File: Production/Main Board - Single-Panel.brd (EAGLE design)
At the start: 186.9 x 99.3 mm, 182 parts, among them J1 MICROMOD-2222-C, J10 MICRO-SD-PUSH-PUSH-EXT-PIN, J11 MICROMOD-2222-C, J12 CORTEX_JTAG_DEBUG_MINIMUM_PTH, J15 MICROMOD_CARRIER, J16 MICRO-SD-PUSH-PUSH-EXT-PIN, J2 Vertical Qwiic Connector, J4 QWIIC_RIGHT_ANGLE, J5 CORTEX_JTAG_DEBUG_MINIMUM_PTH, J6 MICROMOD_CARRIER, J7 Vertical Qwiic Connector, J9 QWIIC_RIGHT_ANGLE, Q1 3.1A/30V/105mΩ, Q2 3.1A/30V/105mΩ, U1 AP7361C-33, U2 MCP73831, U3 MCP73831, U5 AP7361C-33

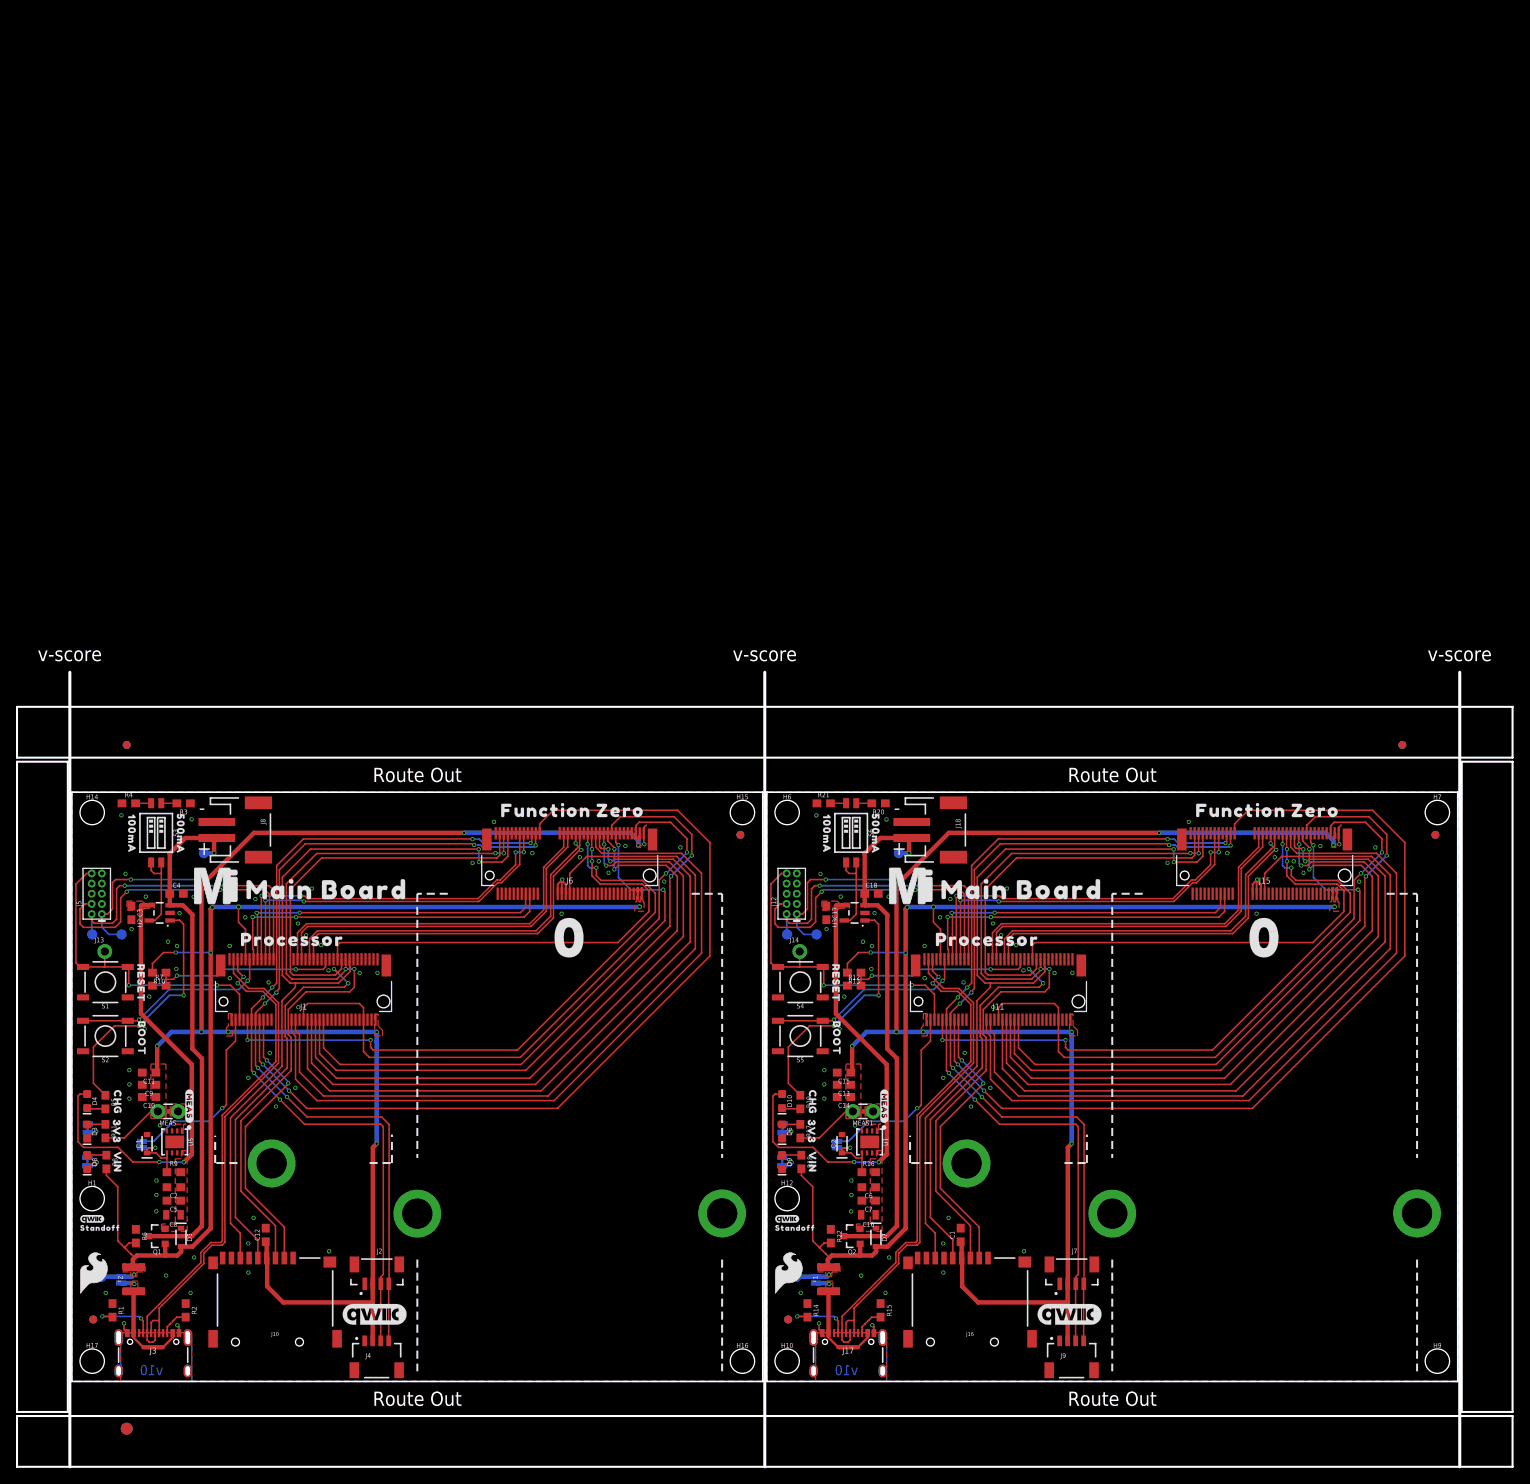
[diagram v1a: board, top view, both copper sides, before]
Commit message: Adds a larger manufacturing panel than the previous
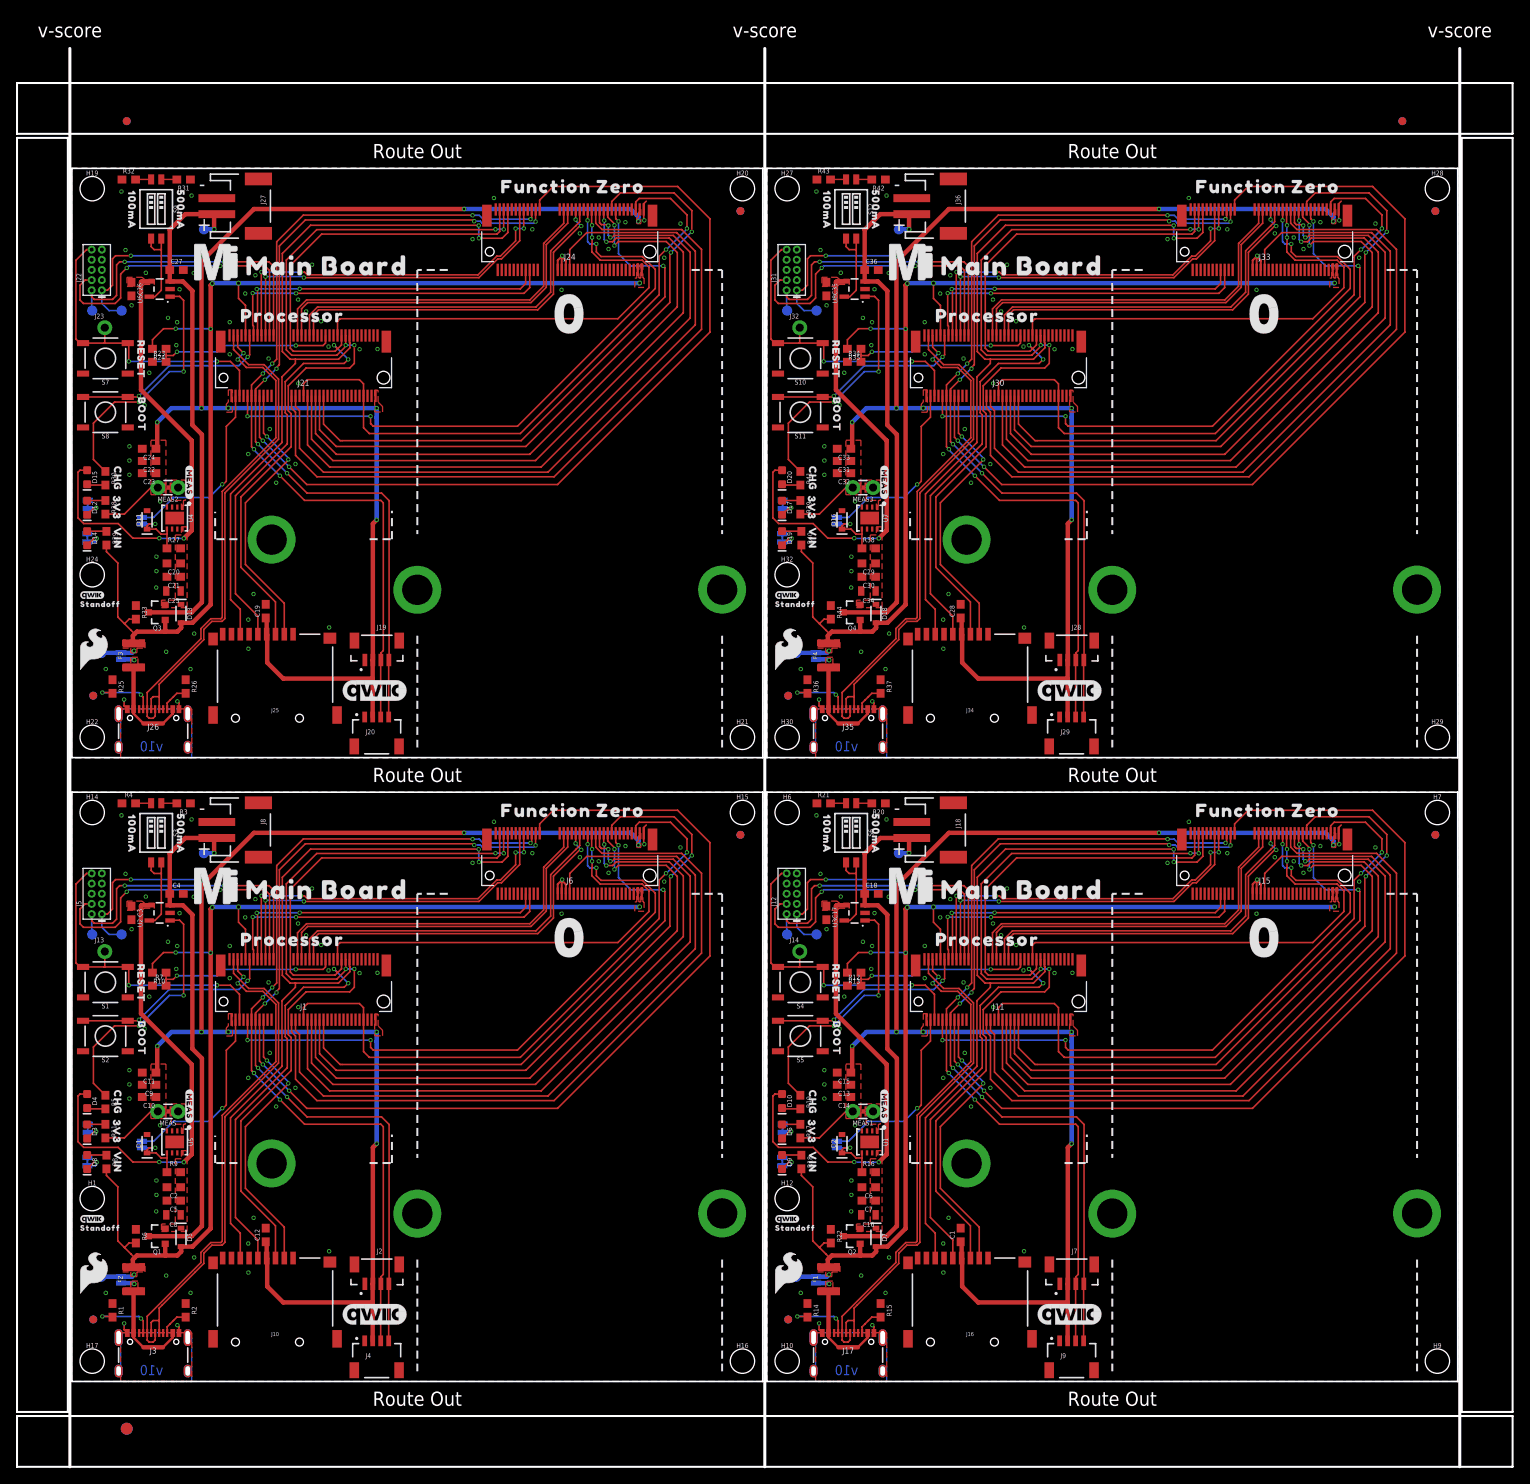
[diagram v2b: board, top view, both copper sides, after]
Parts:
- added 3V3_LED2, 3V3_LED3, 5V_LED2, 5V_LED3: (no value), SparkFun-Jumpers:SMT-JUMPER_2_NC_TRACE_SILK
- added BYP2, BYP3: JUMPER-SMT_2_NO_SILK, SparkFun-Jumpers:SMT-JUMPER_2_NO_SILK
- added C19, C21, C23, C28, C30, C32: 0.1uF, SparkFun-Capacitors:0603
- added C20, C24, C29, C33: 0.22uF, SparkFun-Capacitors:0603
- added C22, C31: 1.0uF, SparkFun-Capacitors:0603
- added C25, C34: 10uF, SparkFun-Capacitors:0805
- added C26, C27, C35, C36: 4.7uF, SparkFun-Capacitors:0603
- added D11, D16: 3.3V, SparkFun-DiscreteSemi:SOD-323
- added D12, D14, D17, D19: RED, SparkFun-LED:LED-0603
- added D13, D18: 3A/10V/280mV, SparkFun-DiscreteSemi:SOD-323
- added D15, D20: Yellow, SparkFun-LED:LED-0603
- added F3, F4: 6V/2A, SparkFun-Fuses:1210
- added FD10, FD11, FD12, FD13, FD14, FD15, FD16, FD9: FIDUCIAL1X2, SparkFun-Aesthetics:FIDUCIAL-1X2
- added H13, H18, H23, H25, H26, H31: STAND-OFF-REFLOW-M2.5_2.5MM_TALL, SparkFun-Hardware:STAND-OFF-REFLOW-M2.5
- added H19, H20, H21, H22, H24, H27, H28, H29, H30, H32: STAND-OFFTIGHT, SparkFun-Hardware:STAND-OFF-TIGHT
- added J19, J28: Vertical Qwiic Connector, SparkFun-Connectors:JST04_1MM_VERT
- added J20, J29: QWIIC_RIGHT_ANGLE, SparkFun-Connectors:JST04_1MM_RA
- added J21, J30: MICROMOD-2222-C, SparkFun-MicroMod:M.2-CONNECTOR-E
- added J22, J31: CORTEX_JTAG_DEBUG_MINIMUM_PTH, SparkFun-Connectors:2X5-PTH-1.27MM
- added J23, J32: (no value), SparkFun-Connectors:1X01_NO_SILK
- added J24, J33: MICROMOD_CARRIER, SparkFun-MicroMod-Function:M.2-CONNECTOR-E-FUNCTION-STANDARD
- added J25, J34: MICRO-SD-PUSH-PUSH-EXT-PIN, SparkFun-Connectors:MICROSD-EXTERNALPIN
- added J26, J35: (no value), SparkFun-Connectors:USB-C-16P-2LAYER-PADS
- added J27, J36: (no value), SparkFun-Connectors:JST-2-SMD
- added LOGO10, LOGO7: QWIIC_LOGO_8MM, SparkFun-Aesthetics:QWIIC_8MM
- added LOGO11, LOGO8: SFE_LOGO_NAME_FLAME.3_INCH, SparkFun-Aesthetics:SFE_LOGO_NAME_FLAME_.3
- added LOGO12, LOGO9: OSHW-LOGOL, SparkFun-Aesthetics:OSHW-LOGO-L
- added MEAS2, MEAS3: JUMPER-COMBO_2_NC_TRACE, SparkFun-Jumpers:COMBO-JUMPER_2_NC_TRACE
- added Q3, Q4: 3.1A/30V/105mΩ, SparkFun-DiscreteSemi:SOT23-3
- added R23, R32, R33, R34, R43, R44: 10k, SparkFun-Resistors:0603
- added R24, R35: 20k, SparkFun-Resistors:0603
- added R25, R26, R36, R37: 5.1k, SparkFun-Resistors:0603
- added R27, R38: 100k, SparkFun-Resistors:0603
- added R28, R30, R39, R41: 1k, SparkFun-Resistors:0603
- added R29, R40: 4.7k, SparkFun-Resistors:0603
- added R31, R42: 2.0k, SparkFun-Resistors:0603
- added S10, S7: Reset, SparkFun-Switches:TACTILE_SWITCH_SMD_5.2MM
- added S11, S8: BOOT, SparkFun-Switches:TACTILE_SWITCH_SMD_5.2MM
- added S12, S9: DIP-02-SMD-50MIL, SparkFun-Switches:DIPSWITCH-02-50MIL
- added TP10, TP11, TP12, TP13, TP14, TP15, TP16, TP9: TEST-POINT3X5, SparkFun-Connectors:PAD.03X.05
- added U$47, U$70: (no value), top:3V332530
- added U$48, U$71: (no value), top:VIN32529
- added U$49, U$72: (no value), top:CHG32528
- added U$50, U$73: (no value), top:FUNCTION_ZERO517
- added U$51, U$74: (no value), top:PROCESSOR522
- added U$52, U$75: (no value), top:#3V3_LED#17
- added U$53, U$76: (no value), top:#VIN_LED#16
- added U$54, U$77: (no value), top:#PTC#18
- added U$55, U$78: (no value), top:BOOT32541
- added U$56, U$79: (no value), top:RESET32540
- added U$57, U$80: (no value), top:#3V3_EN#18
- added U$58, U$81: (no value), SparkFun-MicroMod:MICROMOD_MI_LOGO_1
- added U$59, U$82: (no value), top:0525
- added U$60, U$83: (no value), top:MAIN523
- added U$61, U$84: (no value), top:BOARD524
- added U$62, U$85: (no value), top:100MA6
- added U$63, U$86: (no value), top:500MA101
- added U$64, U$87: (no value), top:MAIN_BOARD5523
- added U$65, U$88: (no value), SparkFun-MicroMod:MICROMOD_LOGO_1
- added U$66, U$89: (no value), SparkFun-Aesthetics:QWIIC_3MM
- added U$67, U$90: (no value), top:STANDOFF501
- added U$68, U$91: (no value), SparkFun-Aesthetics:SFE_LOGO_FLAME_.2
- added U$69, U$92: (no value), top:#MEAS#40313513
- added U4, U7: AP7361C-33, SparkFun-IC-Power:UDFN-8
- added U6, U8: MCP73831, SparkFun-IC-Power:SOT23-5
- added VE2, VE3: (no value), SparkFun-Jumpers:SMT-JUMPER_2_NO_SILK
- moved E$1 78.0 mm to (6.86, 157.5)
- moved E$2 78.0 mm to (6.86, 157.5)
- moved E$3 78.0 mm to (166.3, 157.5)
- moved E$4 78.0 mm to (166.3, 157.5)
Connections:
- new net !BOOT!2: J21.11, S8.3, S8.4
- new net !BOOT!3: J30.11, S11.3, S11.4
- new net !CS0!-PROCESSOR2: J21.55, J24.49
- new net !CS0!-PROCESSOR3: J30.55, J33.49
- new net !RESET!2: J21.6, J22.10, J23.1, S7.3, S7.4
- new net !RESET!3: J30.6, J31.10, J32.1, S10.3, S10.4
- new net 3.3V2: C19.1, C22.1, C23.1, C24.1, J19.2, J20.2, J21.2, J21.74, J22.1, J24.73, J25.4, MEAS2.2, MEAS2.4, R28.2, TP9.1
- new net 3.3V3: C28.1, C31.1, C32.1, C33.1, J28.2, J29.2, J30.2, J30.74, J31.1, J33.73, J34.4, MEAS3.2, MEAS3.4, R39.2, TP13.1
- new net 3.3V_EN2: J21.4, VE2.1
- new net 3.3V_EN3: J30.4, VE3.1
- new net 3.3V_EN_VE2: D11.C, R27.1, U4.5, VE2.2
- new net 3.3V_EN_VE3: D16.C, R38.1, U7.5, VE3.2
- new net A0-PROCESSOR2: J21.34, J24.38
- new net A0-PROCESSOR3: J30.34, J33.38
- new net CTS1-PROCESSOR2: J21.15, J24.16
- new net CTS1-PROCESSOR3: J30.15, J33.16
- new net D+2: J21.3, J26.A6, J26.B6
- new net D+3: J30.3, J35.A6, J35.B6
- new net D-2: J21.5, J26.A7, J26.B7
- new net D-3: J30.5, J35.A7, J35.B7
- new net D0-PROCESSOR2: J21.10, J24.47
- new net D0-PROCESSOR3: J30.10, J33.47
- new net D1-PROCESSOR/SD_CARD_!CS!2: J21.18, J25.2
- new net D1-PROCESSOR/SD_CARD_!CS!3: J30.18, J34.2
- new net G0-PROCESSOR2: J21.40, J24.53
- new net G0-PROCESSOR3: J30.40, J33.53
- new net G1-PROCESSOR2: J21.42, J24.55
- new net G1-PROCESSOR3: J30.42, J33.55
- new net G2-PROCESSOR2: J21.44, J24.57
- new net G2-PROCESSOR3: J30.44, J33.57
- new net G3-PROCESSOR2: J21.46, J24.59
- new net G3-PROCESSOR3: J30.46, J33.59
- new net G4-PROCESSOR2: J21.48, J24.61
- new net G4-PROCESSOR3: J30.48, J33.61
- new net GND2: 3V3_LED2.1, 5V_LED2.1, C19.2, C20.2, C21.2, C22.2, C23.2, C24.2, C25.2, C26.2, C27.2, D11.A, H13.1, H18.1, H23.1, J19.1, J20.1, J21.1, J21.33, J21.36, J21.39, J21.45, J21.7, J21.75, J22.3, J22.5, J22.9, J24.1, J24.32, J24.33, J24.34, J24.36, J24.39, J24.45, J24.75, J25.10, J25.11, J25.12, J25.13, J25.6, J26.GND, J26.GND2, J27.1, R23.1, R25.1, R26.1, R31.1, R32.1, R33.1, S7.1, S7.2, S8.1, S8.2, U4.4, U4.EP, U6.2
- new net GND3: 3V3_LED3.1, 5V_LED3.1, C28.2, C29.2, C30.2, C31.2, C32.2, C33.2, C34.2, C35.2, C36.2, D16.A, H25.1, H26.1, H31.1, J28.1, J29.1, J30.1, J30.33, J30.36, J30.39, J30.45, J30.7, J30.75, J31.3, J31.5, J31.9, J33.1, J33.32, J33.33, J33.34, J33.36, J33.39, J33.45, J33.75, J34.10, J34.11, J34.12, J34.13, J34.6, J35.GND, J35.GND2, J36.1, R34.1, R36.1, R37.1, R42.1, R43.1, R44.1, S10.1, S10.2, S11.1, S11.2, U7.4, U7.EP, U8.2
- new net HOST_D+2: J21.35, J24.35
- new net HOST_D+3: J30.35, J33.35
- new net HOST_D-2: J21.37, J24.37
- new net HOST_D-3: J30.37, J33.37
- new net I2C_!INT!2: J21.16, J24.23
- new net I2C_!INT!3: J30.16, J33.23
- new net I2C_SCL2: J19.4, J20.4, J21.14, J24.21
- new net I2C_SCL3: J28.4, J29.4, J30.14, J33.21
- new net I2C_SDA2: J19.3, J20.3, J21.12, J24.19
- new net I2C_SDA3: J28.3, J29.3, J30.12, J33.19
- new net N$27: J26.B5, R26.2
- new net N$28: J26.A5, R25.2
- new net N$29: MEAS2.1, MEAS2.3, U4.1
- new net N$30: D12.A, R28.1
- new net N$31: BYP2.1, F3.1, J26.VBUS1, J26.VBUS2
- new net N$32: D14.A, R29.1
- new net N$33: 5V_LED2.2, D14.C
- new net N$34: 3V3_LED2.2, D12.C
- new net N$35: S9.3, S9.4, U6.5
- new net N$36: D15.C, R30.2
- new net N$37: R30.1, U6.1
- new net N$38: R31.2, S9.1
- new net N$39: R32.2, S9.2
- new net N$40: J35.B5, R37.2
- new net N$41: J35.A5, R36.2
- new net N$42: MEAS3.1, MEAS3.3, U7.1
- new net N$43: D17.A, R39.1
- new net N$44: BYP3.1, F4.1, J35.VBUS1, J35.VBUS2
- new net N$45: D19.A, R40.1
- new net N$46: 5V_LED3.2, D19.C
- new net N$47: 3V3_LED3.2, D17.C
- new net N$48: S12.3, S12.4, U8.5
- new net N$49: D20.C, R41.2
- new net N$50: R41.1, U8.1
- new net N$51: R42.2, S12.1
- new net N$52: R43.2, S12.2
- new net PROCESSOR_CAN-RX2: J21.41, J24.43
- new net PROCESSOR_CAN-RX3: J30.41, J33.43
- new net PROCESSOR_CAN-TX2: J21.43, J24.41
- new net PROCESSOR_CAN-TX3: J30.43, J33.41
- new net PWM0-PROCESSOR2: J21.32, J24.51
- new net PWM0-PROCESSOR3: J30.32, J33.51
- new net PWR_EN2: J21.38, J21.68, J24.71
- new net PWR_EN3: J30.38, J30.68, J33.71
- new net RTS1-PROCESSOR2: J21.13, J24.18
- new net RTS1-PROCESSOR3: J30.13, J33.18
- new net RX1-PROCESSOR2: J21.19, J24.13
- new net RX1-PROCESSOR3: J30.19, J33.13
- new net SPI_PROCESSOR_SCK2: J21.57, J24.3, J25.5
- new net SPI_PROCESSOR_SCK3: J30.57, J33.3, J34.5
- new net SPI_PROCESSOR_SDI2: J21.61, J24.7, J25.7
- new net SPI_PROCESSOR_SDI3: J30.61, J33.7, J34.7
- new net SPI_PROCESSOR_SDO2: J21.59, J24.5, J25.3
- new net SPI_PROCESSOR_SDO3: J30.59, J33.5, J34.3
- new net SWDCK2: J21.21, J22.4
- new net SWDCK3: J30.21, J31.4
- new net SWDIO2: J21.23, J22.2, TP12.1
- new net SWDIO3: J30.23, J31.2, TP16.1
- new net TX1-PROCESSOR2: J21.17, J24.15
- new net TX1-PROCESSOR3: J30.17, J33.15
- new net VCC2: C20.1, C21.1, C25.1, C26.1, D13.C, D15.A, Q3.2, R27.2, U4.8, U6.4
- new net VCC3: C29.1, C30.1, C34.1, C35.1, D18.C, D20.A, Q4.2, R38.2, U7.8, U8.4
- new net VIN/2: J21.49, R23.2, R24.1
- new net VIN/4: J30.49, R34.2, R35.1
- new net VIN2: BYP2.2, D13.A, F3.2, J21.9, J24.72, J24.74, Q3.1, R24.2, R29.2, R33.2, TP11.1
- new net VIN3: BYP3.2, D18.A, F4.2, J30.9, J33.72, J33.74, Q4.1, R35.2, R40.2, R44.2, TP15.1
- new net V_BATT2: C27.1, J27.2, Q3.3, TP10.1, U6.3
- new net V_BATT3: C36.1, J36.2, Q4.3, TP14.1, U8.3
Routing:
- net 3.3V3: track 0.00 -> 195.7 mm, vias 0 -> 9
- net 3.3V2: track 0.00 -> 195.7 mm, vias 0 -> 9
- net VIN2: track 0.00 -> 142.2 mm, vias 0 -> 6
- net VIN3: track 0.00 -> 142.2 mm, vias 0 -> 6
- net I2C_!INT!3: track 0.00 -> 110.8 mm, vias 0 -> 2
- net I2C_!INT!2: track 0.00 -> 110.8 mm, vias 0 -> 2
- net I2C_SDA2: track 0.00 -> 107.9 mm, vias 0 -> 6
- net I2C_SDA3: track 0.00 -> 107.9 mm, vias 0 -> 6
- net I2C_SCL3: track 0.00 -> 107.7 mm, vias 0 -> 6
- net I2C_SCL2: track 0.00 -> 107.7 mm, vias 0 -> 6
- net SPI_PROCESSOR_SDO3: track 0.00 -> 100.4 mm, vias 0 -> 4
- net SPI_PROCESSOR_SDO2: track 0.00 -> 100.4 mm, vias 0 -> 4
- net SPI_PROCESSOR_SCK3: track 0.00 -> 96.8 mm, vias 0 -> 2
- net SPI_PROCESSOR_SCK2: track 0.00 -> 96.8 mm, vias 0 -> 2
- net SPI_PROCESSOR_SDI2: track 0.00 -> 95.9 mm, vias 0 -> 2
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- added copper zone on layer 1, net 3.3V2
- added copper zone on layer 1, net 3.3V3
- added copper zone on layer 1, net GND2
- added copper zone on layer 16, net GND2
- added copper zone on layer 1, net GND3
- added copper zone on layer 16, net GND3
- added copper zone on layer 1, net N$29
- added copper zone on layer 1, net N$31
- added copper zone on layer 1, net N$42
- added copper zone on layer 1, net N$44
- added copper zone on layer 1, net SHLD2
- added copper zone on layer 16, net SHLD2
- added copper zone on layer 1, net SHLD3
- added copper zone on layer 16, net SHLD3
- added copper zone on layer 1, net VCC2
- added copper zone on layer 1, net VCC3
- added copper zone on layer 1, net VIN2
- added copper zone on layer 1, net VIN3
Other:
- board size 186.9 x 99.3 mm -> 186.9 x 177.3 mm

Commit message: Adds new panel that is two columns of three
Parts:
- added 3V3_LED4, 3V3_LED5, 5V_LED4, 5V_LED5: (no value), SparkFun-Jumpers:SMT-JUMPER_2_NC_TRACE_SILK
- added BYP4, BYP5: JUMPER-SMT_2_NO_SILK, SparkFun-Jumpers:SMT-JUMPER_2_NO_SILK
- added C37, C39, C41, C46, C48, C50: 0.1uF, SparkFun-Capacitors:0603
- added C38, C42, C47, C51: 0.22uF, SparkFun-Capacitors:0603
- added C40, C49: 1.0uF, SparkFun-Capacitors:0603
- added C43, C52: 10uF, SparkFun-Capacitors:0805
- added C44, C45, C53, C54: 4.7uF, SparkFun-Capacitors:0603
- added D21, D26: 3.3V, SparkFun-DiscreteSemi:SOD-323
- added D22, D24, D27, D29: RED, SparkFun-LED:LED-0603
- added D23, D28: 3A/10V/280mV, SparkFun-DiscreteSemi:SOD-323
- added D25, D30: Yellow, SparkFun-LED:LED-0603
- added F5, F6: 6V/2A, SparkFun-Fuses:1210
- added FD17, FD18, FD19, FD20, FD21, FD22, FD23, FD24: FIDUCIAL1X2, SparkFun-Aesthetics:FIDUCIAL-1X2
- added H33, H34, H39, H41, H42, H47: STAND-OFF-REFLOW-M2.5_2.5MM_TALL, SparkFun-Hardware:STAND-OFF-REFLOW-M2.5
- added H35, H36, H37, H38, H40, H43, H44, H45, H46, H48: STAND-OFFTIGHT, SparkFun-Hardware:STAND-OFF-TIGHT
- added J37, J46: Vertical Qwiic Connector, SparkFun-Connectors:JST04_1MM_VERT
- added J38, J47: QWIIC_RIGHT_ANGLE, SparkFun-Connectors:JST04_1MM_RA
- added J39, J48: MICROMOD-2222-C, SparkFun-MicroMod:M.2-CONNECTOR-E
- added J40, J49: CORTEX_JTAG_DEBUG_MINIMUM_PTH, SparkFun-Connectors:2X5-PTH-1.27MM
- added J41, J50: (no value), SparkFun-Connectors:1X01_NO_SILK
- added J42, J51: MICROMOD_CARRIER, SparkFun-MicroMod-Function:M.2-CONNECTOR-E-FUNCTION-STANDARD
- added J43, J52: MICRO-SD-PUSH-PUSH-EXT-PIN, SparkFun-Connectors:MICROSD-EXTERNALPIN
- added J44, J53: (no value), SparkFun-Connectors:USB-C-16P-2LAYER-PADS
- added J45, J54: (no value), SparkFun-Connectors:JST-2-SMD
- added LOGO13, LOGO16: QWIIC_LOGO_8MM, SparkFun-Aesthetics:QWIIC_8MM
- added LOGO14, LOGO17: SFE_LOGO_NAME_FLAME.3_INCH, SparkFun-Aesthetics:SFE_LOGO_NAME_FLAME_.3
- added LOGO15, LOGO18: OSHW-LOGOL, SparkFun-Aesthetics:OSHW-LOGO-L
- added MEAS4, MEAS5: JUMPER-COMBO_2_NC_TRACE, SparkFun-Jumpers:COMBO-JUMPER_2_NC_TRACE
- added Q5, Q6: 3.1A/30V/105mΩ, SparkFun-DiscreteSemi:SOT23-3
- added R45, R54, R55, R56, R65, R66: 10k, SparkFun-Resistors:0603
- added R46, R57: 20k, SparkFun-Resistors:0603
- added R47, R48, R58, R59: 5.1k, SparkFun-Resistors:0603
- added R49, R60: 100k, SparkFun-Resistors:0603
- added R50, R52, R61, R63: 1k, SparkFun-Resistors:0603
- added R51, R62: 4.7k, SparkFun-Resistors:0603
- added R53, R64: 2.0k, SparkFun-Resistors:0603
- added S13, S16: Reset, SparkFun-Switches:TACTILE_SWITCH_SMD_5.2MM
- added S14, S17: BOOT, SparkFun-Switches:TACTILE_SWITCH_SMD_5.2MM
- added S15, S18: DIP-02-SMD-50MIL, SparkFun-Switches:DIPSWITCH-02-50MIL
- added TP17, TP18, TP19, TP20, TP21, TP22, TP23, TP24: TEST-POINT3X5, SparkFun-Connectors:PAD.03X.05
- added U$100, U$123: (no value), top:#PTC#18
- added U$101, U$124: (no value), top:BOOT32541
- added U$102, U$125: (no value), top:RESET32540
- added U$103, U$126: (no value), top:#3V3_EN#18
- added U$104, U$127: (no value), SparkFun-MicroMod:MICROMOD_MI_LOGO_1
- added U$105, U$128: (no value), top:0525
- added U$106, U$129: (no value), top:MAIN523
- added U$107, U$130: (no value), top:BOARD524
- added U$108, U$131: (no value), top:100MA6
- added U$109, U$132: (no value), top:500MA101
- added U$110, U$133: (no value), top:MAIN_BOARD5523
- added U$111, U$134: (no value), SparkFun-MicroMod:MICROMOD_LOGO_1
- added U$112, U$135: (no value), SparkFun-Aesthetics:QWIIC_3MM
- added U$113, U$136: (no value), top:STANDOFF501
- added U$114, U$137: (no value), SparkFun-Aesthetics:SFE_LOGO_FLAME_.2
- added U$115, U$138: (no value), top:#MEAS#40313513
- added U$116, U$93: (no value), top:3V332530
- added U$117, U$94: (no value), top:VIN32529
- added U$118, U$95: (no value), top:CHG32528
- added U$119, U$96: (no value), top:FUNCTION_ZERO517
- added U$120, U$97: (no value), top:PROCESSOR522
- added U$121, U$98: (no value), top:#3V3_LED#17
- added U$122, U$99: (no value), top:#VIN_LED#16
- added U10, U12: MCP73831, SparkFun-IC-Power:SOT23-5
- added U11, U9: AP7361C-33, SparkFun-IC-Power:UDFN-8
- added VE4, VE5: (no value), SparkFun-Jumpers:SMT-JUMPER_2_NO_SILK
- moved E$3 73.8 mm to (175.9, 230.8)
- moved E$4 73.8 mm to (175.9, 230.8)
- moved E$1 73.8 mm to (-2.62, 230.8)
- moved E$2 73.8 mm to (-2.62, 230.8)
- moved E$5 15.5 mm to (-2.62, 6.35)
- moved E$6 15.5 mm to (-2.62, 6.35)
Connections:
- new net !BOOT!4: J39.11, S14.3, S14.4
- new net !BOOT!5: J48.11, S17.3, S17.4
- new net !CS0!-PROCESSOR4: J39.55, J42.49
- new net !CS0!-PROCESSOR5: J48.55, J51.49
- new net !RESET!4: J39.6, J40.10, J41.1, S13.3, S13.4
- new net !RESET!5: J48.6, J49.10, J50.1, S16.3, S16.4
- new net 3.3V4: C37.1, C40.1, C41.1, C42.1, J37.2, J38.2, J39.2, J39.74, J40.1, J42.73, J43.4, MEAS4.2, MEAS4.4, R50.2, TP17.1
- new net 3.3V5: C46.1, C49.1, C50.1, C51.1, J46.2, J47.2, J48.2, J48.74, J49.1, J51.73, J52.4, MEAS5.2, MEAS5.4, R61.2, TP21.1
- new net 3.3V_EN4: J39.4, VE4.1
- new net 3.3V_EN5: J48.4, VE5.1
- new net 3.3V_EN_VE4: D21.C, R49.1, U9.5, VE4.2
- new net 3.3V_EN_VE5: D26.C, R60.1, U11.5, VE5.2
- new net A0-PROCESSOR4: J39.34, J42.38
- new net A0-PROCESSOR5: J48.34, J51.38
- new net CTS1-PROCESSOR4: J39.15, J42.16
- new net CTS1-PROCESSOR5: J48.15, J51.16
- new net D+4: J39.3, J44.A6, J44.B6
- new net D+5: J48.3, J53.A6, J53.B6
- new net D-4: J39.5, J44.A7, J44.B7
- new net D-5: J48.5, J53.A7, J53.B7
- new net D0-PROCESSOR4: J39.10, J42.47
- new net D0-PROCESSOR5: J48.10, J51.47
- new net D1-PROCESSOR/SD_CARD_!CS!4: J39.18, J43.2
- new net D1-PROCESSOR/SD_CARD_!CS!5: J48.18, J52.2
- new net G0-PROCESSOR4: J39.40, J42.53
- new net G0-PROCESSOR5: J48.40, J51.53
- new net G1-PROCESSOR4: J39.42, J42.55
- new net G1-PROCESSOR5: J48.42, J51.55
- new net G2-PROCESSOR4: J39.44, J42.57
- new net G2-PROCESSOR5: J48.44, J51.57
- new net G3-PROCESSOR4: J39.46, J42.59
- new net G3-PROCESSOR5: J48.46, J51.59
- new net G4-PROCESSOR4: J39.48, J42.61
- new net G4-PROCESSOR5: J48.48, J51.61
- new net GND4: 3V3_LED4.1, 5V_LED4.1, C37.2, C38.2, C39.2, C40.2, C41.2, C42.2, C43.2, C44.2, C45.2, D21.A, H33.1, H34.1, H39.1, J37.1, J38.1, J39.1, J39.33, J39.36, J39.39, J39.45, J39.7, J39.75, J40.3, J40.5, J40.9, J42.1, J42.32, J42.33, J42.34, J42.36, J42.39, J42.45, J42.75, J43.10, J43.11, J43.12, J43.13, J43.6, J44.GND, J44.GND2, J45.1, R45.1, R47.1, R48.1, R53.1, R54.1, R55.1, S13.1, S13.2, S14.1, S14.2, U10.2, U9.4, U9.EP
- new net GND5: 3V3_LED5.1, 5V_LED5.1, C46.2, C47.2, C48.2, C49.2, C50.2, C51.2, C52.2, C53.2, C54.2, D26.A, H41.1, H42.1, H47.1, J46.1, J47.1, J48.1, J48.33, J48.36, J48.39, J48.45, J48.7, J48.75, J49.3, J49.5, J49.9, J51.1, J51.32, J51.33, J51.34, J51.36, J51.39, J51.45, J51.75, J52.10, J52.11, J52.12, J52.13, J52.6, J53.GND, J53.GND2, J54.1, R56.1, R58.1, R59.1, R64.1, R65.1, R66.1, S16.1, S16.2, S17.1, S17.2, U11.4, U11.EP, U12.2
- new net HOST_D+4: J39.35, J42.35
- new net HOST_D+5: J48.35, J51.35
- new net HOST_D-4: J39.37, J42.37
- new net HOST_D-5: J48.37, J51.37
- new net I2C_!INT!4: J39.16, J42.23
- new net I2C_!INT!5: J48.16, J51.23
- new net I2C_SCL4: J37.4, J38.4, J39.14, J42.21
- new net I2C_SCL5: J46.4, J47.4, J48.14, J51.21
- new net I2C_SDA4: J37.3, J38.3, J39.12, J42.19
- new net I2C_SDA5: J46.3, J47.3, J48.12, J51.19
- new net N$53: J44.B5, R48.2
- new net N$54: J44.A5, R47.2
- new net N$55: MEAS4.1, MEAS4.3, U9.1
- new net N$56: D22.A, R50.1
- new net N$57: BYP4.1, F5.1, J44.VBUS1, J44.VBUS2
- new net N$58: D24.A, R51.1
- new net N$59: 5V_LED4.2, D24.C
- new net N$60: 3V3_LED4.2, D22.C
- new net N$61: S15.3, S15.4, U10.5
- new net N$62: D25.C, R52.2
- new net N$63: R52.1, U10.1
- new net N$64: R53.2, S15.1
- new net N$65: R54.2, S15.2
- new net N$66: J53.B5, R59.2
- new net N$67: J53.A5, R58.2
- new net N$68: MEAS5.1, MEAS5.3, U11.1
- new net N$69: D27.A, R61.1
- new net N$70: BYP5.1, F6.1, J53.VBUS1, J53.VBUS2
- new net N$71: D29.A, R62.1
- new net N$72: 5V_LED5.2, D29.C
- new net N$73: 3V3_LED5.2, D27.C
- new net N$74: S18.3, S18.4, U12.5
- new net N$75: D30.C, R63.2
- new net N$76: R63.1, U12.1
- new net N$77: R64.2, S18.1
- new net N$78: R65.2, S18.2
- new net PROCESSOR_CAN-RX4: J39.41, J42.43
- new net PROCESSOR_CAN-RX5: J48.41, J51.43
- new net PROCESSOR_CAN-TX4: J39.43, J42.41
- new net PROCESSOR_CAN-TX5: J48.43, J51.41
- new net PWM0-PROCESSOR4: J39.32, J42.51
- new net PWM0-PROCESSOR5: J48.32, J51.51
- new net PWR_EN4: J39.38, J39.68, J42.71
- new net PWR_EN5: J48.38, J48.68, J51.71
- new net RTS1-PROCESSOR4: J39.13, J42.18
- new net RTS1-PROCESSOR5: J48.13, J51.18
- new net RX1-PROCESSOR4: J39.19, J42.13
- new net RX1-PROCESSOR5: J48.19, J51.13
- new net SPI_PROCESSOR_SCK4: J39.57, J42.3, J43.5
- new net SPI_PROCESSOR_SCK5: J48.57, J51.3, J52.5
- new net SPI_PROCESSOR_SDI4: J39.61, J42.7, J43.7
- new net SPI_PROCESSOR_SDI5: J48.61, J51.7, J52.7
- new net SPI_PROCESSOR_SDO4: J39.59, J42.5, J43.3
- new net SPI_PROCESSOR_SDO5: J48.59, J51.5, J52.3
- new net SWDCK4: J39.21, J40.4
- new net SWDCK5: J48.21, J49.4
- new net SWDIO4: J39.23, J40.2, TP20.1
- new net SWDIO5: J48.23, J49.2, TP24.1
- new net TX1-PROCESSOR4: J39.17, J42.15
- new net TX1-PROCESSOR5: J48.17, J51.15
- new net VCC4: C38.1, C39.1, C43.1, C44.1, D23.C, D25.A, Q5.2, R49.2, U10.4, U9.8
- new net VCC5: C47.1, C48.1, C52.1, C53.1, D28.C, D30.A, Q6.2, R60.2, U11.8, U12.4
- new net VIN/5: J39.49, R45.2, R46.1
- new net VIN/6: J48.49, R56.2, R57.1
- new net VIN4: BYP4.2, D23.A, F5.2, J39.9, J42.72, J42.74, Q5.1, R46.2, R51.2, R55.2, TP19.1
- new net VIN5: BYP5.2, D28.A, F6.2, J48.9, J51.72, J51.74, Q6.1, R57.2, R62.2, R66.2, TP23.1
- new net V_BATT4: C45.1, J45.2, Q5.3, TP18.1, U10.3
- new net V_BATT5: C54.1, J54.2, Q6.3, TP22.1, U12.3
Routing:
- net 3.3V4: track 0.00 -> 195.7 mm, vias 0 -> 9
- net 3.3V5: track 0.00 -> 195.7 mm, vias 0 -> 9
- net VIN5: track 0.00 -> 142.2 mm, vias 0 -> 6
- net VIN4: track 0.00 -> 142.2 mm, vias 0 -> 6
- net I2C_!INT!5: track 0.00 -> 110.8 mm, vias 0 -> 2
- net I2C_!INT!4: track 0.00 -> 110.8 mm, vias 0 -> 2
- net I2C_SDA4: track 0.00 -> 107.9 mm, vias 0 -> 6
- net I2C_SDA5: track 0.00 -> 107.9 mm, vias 0 -> 6
- net I2C_SCL5: track 0.00 -> 107.7 mm, vias 0 -> 6
- net I2C_SCL4: track 0.00 -> 107.7 mm, vias 0 -> 6
- net SPI_PROCESSOR_SDO5: track 0.00 -> 100.4 mm, vias 0 -> 4
- net SPI_PROCESSOR_SDO4: track 0.00 -> 100.4 mm, vias 0 -> 4
- net SPI_PROCESSOR_SCK5: track 0.00 -> 96.8 mm, vias 0 -> 2
- net SPI_PROCESSOR_SCK4: track 0.00 -> 96.8 mm, vias 0 -> 2
- net SPI_PROCESSOR_SDI4: track 0.00 -> 95.9 mm, vias 0 -> 2
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- added copper zone on layer 1, net 3.3V4
- added copper zone on layer 1, net 3.3V5
- added copper zone on layer 1, net GND4
- added copper zone on layer 16, net GND4
- added copper zone on layer 1, net GND5
- added copper zone on layer 16, net GND5
- added copper zone on layer 1, net N$55
- added copper zone on layer 1, net N$57
- added copper zone on layer 1, net N$68
- added copper zone on layer 1, net N$70
- added copper zone on layer 1, net SHLD4
- added copper zone on layer 16, net SHLD4
- added copper zone on layer 1, net SHLD5
- added copper zone on layer 16, net SHLD5
- added copper zone on layer 1, net VCC4
- added copper zone on layer 1, net VCC5
- added copper zone on layer 1, net VIN4
- added copper zone on layer 1, net VIN5
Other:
- board size 186.9 x 177.3 mm -> 186.9 x 255.3 mm
